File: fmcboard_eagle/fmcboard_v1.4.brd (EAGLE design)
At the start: 147 x 74 mm, 160 parts, among them IC1 OPA699ID, IC10 LTC6229IMS8E#TRPBF, IC11 7805TV, IC12 SN74AUC2G66DCTR, IC13 SN74AUC2G66DCTR, IC14 SN74AUC2G66DCTR, IC15 SN74AUC2G66DCTR, IC16 DAC7578SPWR, IC2 DAC7578SPWR, IC3 LTC6229IMS8E#TRPBF, IC4 LTC6229IMS8E#TRPBF, IC5 LM358, IC6 OPA699ID, IC7 OPA699ID, IC8 LTC6229IMS8E#TRPBF, IC9 LTC6229IMS8E#TRPBF, J1 8pin, J10 8pin, J12 4p-2.54, J2 ASP-134604-01, J3 4p-2.54, J4 4p-2.54, J5 8pin, J6 4p-2.54, J7 4p-2.54, J8 4p-2.54, J9 8pin, U1 TXS0108EPWR, U2 STMICROELECTRONICS_L7905ACVST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

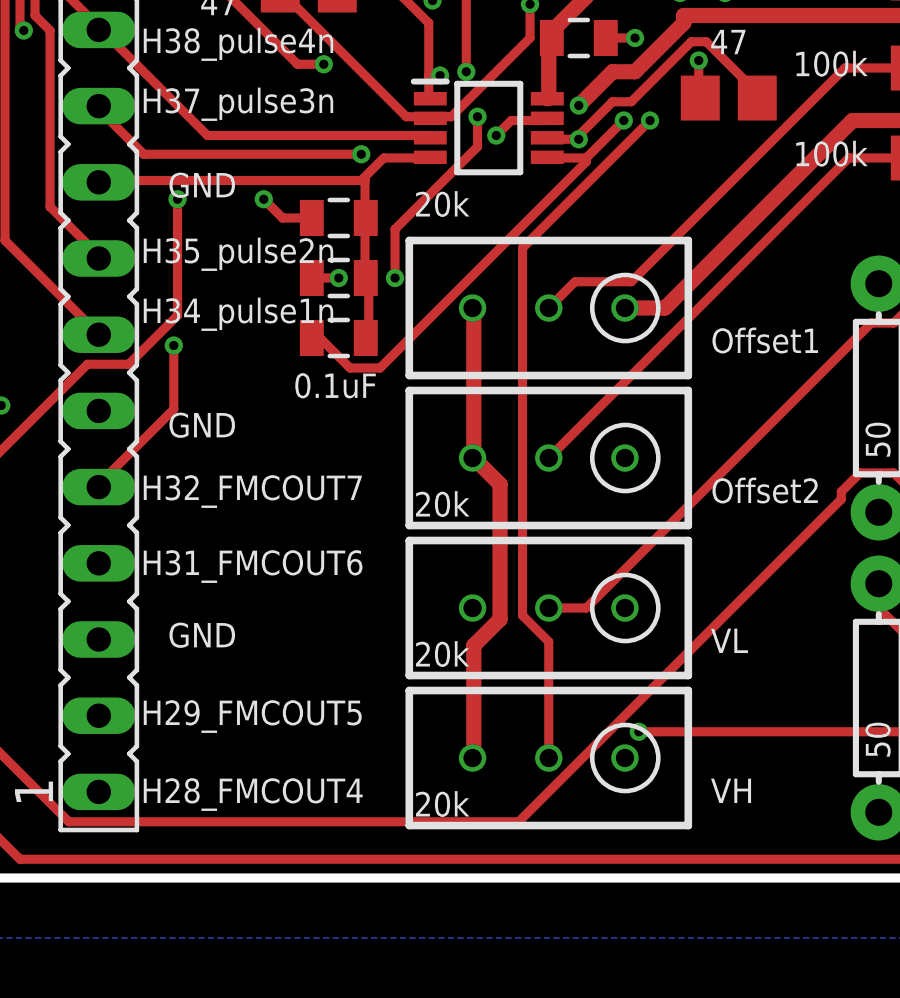
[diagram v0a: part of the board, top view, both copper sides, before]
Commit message: 20k -> 5k pots
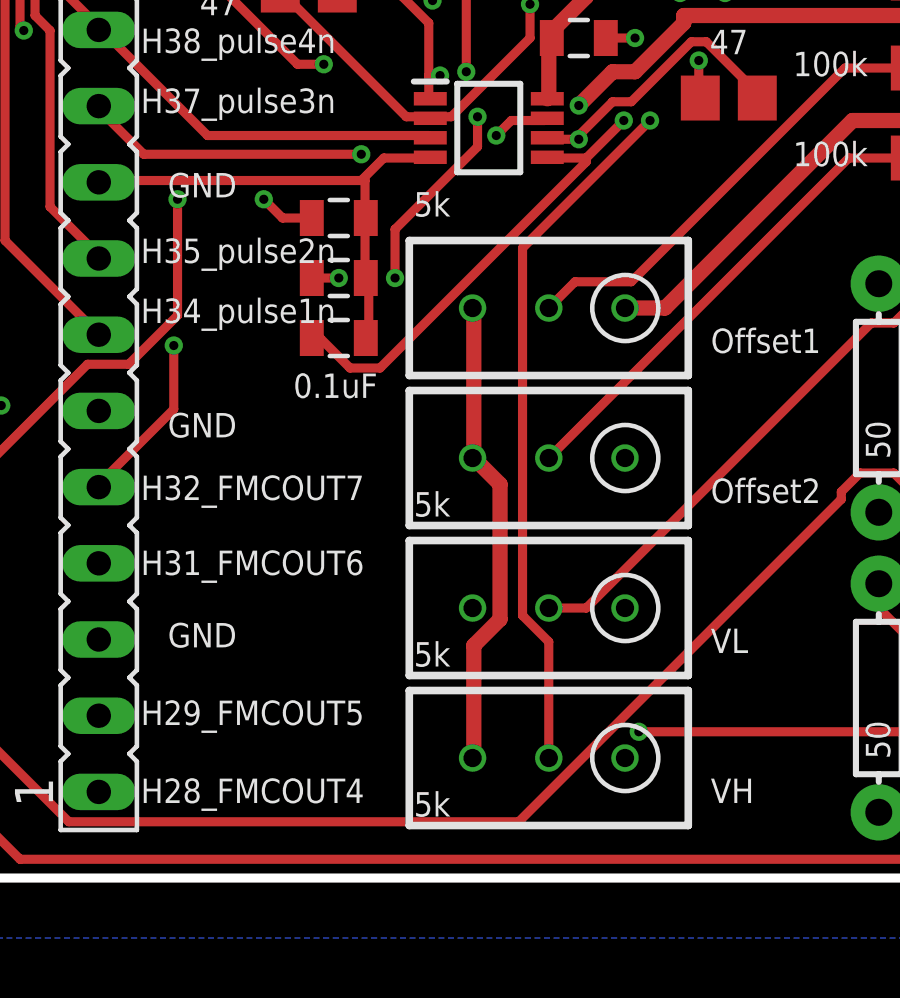
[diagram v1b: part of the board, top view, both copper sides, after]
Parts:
- R_O1, R_O2, R_VH, R_VL: value 20k -> 5k
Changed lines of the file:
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@@
 <element name="C13" library="SparkFun-Passives" package="0805" value="0.1uF" x="54" y="67" smashed="yes"/>
 <element name="C14" library="SparkFun-Passives" package="0805" value="0.1uF" x="96" y="2" smashed="yes" rot="R180"/>
-<element name="R_VH" library="resistor" library_urn="urn:adsk.eagle:library:348" package="RTRIM3296W" package3d_urn="urn:adsk.eagle:package:26033/1" value="20k" x="43" y="4" smashed="yes" rot="R90">
+<element name="R_VH" library="resistor" library_urn="urn:adsk.eagle:library:348" package="RTRIM3296W" package3d_urn="urn:adsk.eagle:package:26033/1" value="5k" x="43" y="4" smashed="yes" rot="R90">
 <attribute name="VALUE" x="38.5" y="2.05" size="0.8128" layer="21"/>
 </element>
-<element name="R_VL" library="resistor" library_urn="urn:adsk.eagle:library:348" package="RTRIM3296W" package3d_urn="urn:adsk.eagle:package:26033/1" value="20k" x="43" y="9" smashed="yes" rot="R90">
+<element name="R_VL" library="resistor" library_urn="urn:adsk.eagle:library:348" package="RTRIM3296W" package3d_urn="urn:adsk.eagle:package:26033/1" value="5k" x="43" y="9" smashed="yes" rot="R90">
 <attribute name="VALUE" x="38.5" y="7.05" size="0.8128" layer="21"/>
 </element>
@@
 <attribute name="VALUE" x="73.635" y="45.54" size="0.8128" layer="21" rot="R180"/>
 </element>
-<element name="R_O1" library="resistor" library_urn="urn:adsk.eagle:library:348" package="RTRIM3296W" package3d_urn="urn:adsk.eagle:package:26033/1" value="20k" x="43" y="19" smashed="yes" rot="R90">
+<element name="R_O1" library="resistor" library_urn="urn:adsk.eagle:library:348" package="RTRIM3296W" package3d_urn="urn:adsk.eagle:package:26033/1" value="5k" x="43" y="19" smashed="yes" rot="R90">
 <attribute name="VALUE" x="38.5" y="22.05" size="0.8128" layer="21"/>
 </element>
@@
 </element>
 <element name="C4" library="SparkFun-Passives" package="0805" value="0.1uF" x="69" y="24" smashed="yes"/>
-<element name="R_O2" library="resistor" library_urn="urn:adsk.eagle:library:348" package="RTRIM3296W" package3d_urn="urn:adsk.eagle:package:26033/1" value="20k" x="43" y="14" smashed="yes" rot="R90">
+<element name="R_O2" library="resistor" library_urn="urn:adsk.eagle:library:348" package="RTRIM3296W" package3d_urn="urn:adsk.eagle:package:26033/1" value="5k" x="43" y="14" smashed="yes" rot="R90">
 <attribute name="VALUE" x="38.5" y="12.05" size="0.8128" layer="21"/>
 </element>

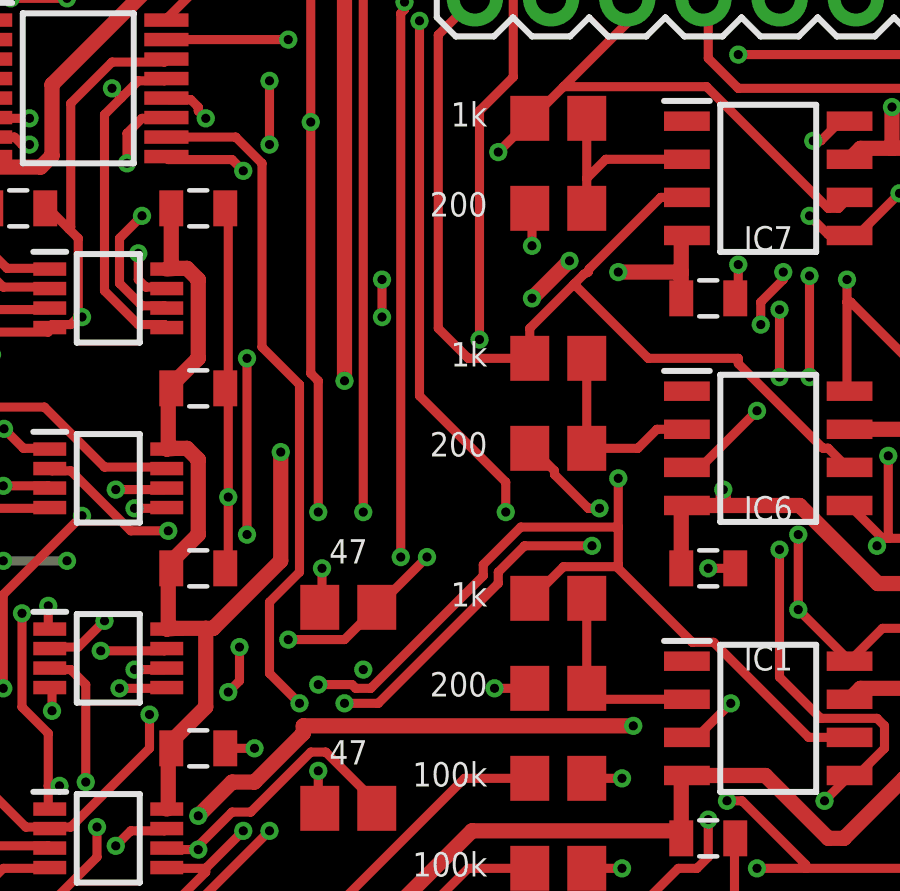
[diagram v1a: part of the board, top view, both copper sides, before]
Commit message: Gain resistors updated to 1k, 100
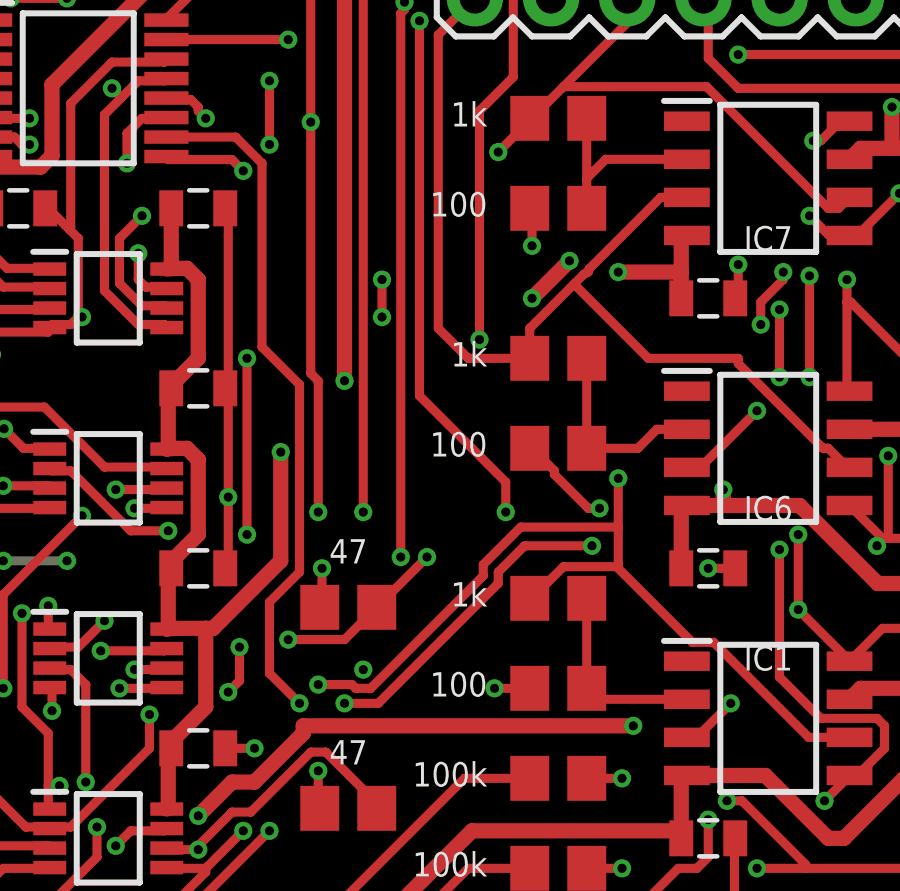
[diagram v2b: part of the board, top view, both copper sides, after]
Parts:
- R10, R19, R26: value 200 -> 100
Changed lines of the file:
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@@
 <attribute name="VALUE" x="53.635" y="33.54" size="0.8128" layer="21" rot="R180"/>
 </element>
-<element name="R10" library="rcl" library_urn="urn:adsk.eagle:library:334" package="R0805" package3d_urn="urn:adsk.eagle:package:23553/2" value="200" x="56" y="30" smashed="yes">
+<element name="R10" library="rcl" library_urn="urn:adsk.eagle:library:334" package="R0805" package3d_urn="urn:adsk.eagle:package:23553/2" value="100" x="56" y="30" smashed="yes">
 <attribute name="POPULARITY" value="85" x="56" y="30" size="1.778" layer="27" display="off"/>
 <attribute name="SPICEPREFIX" value="R" x="56" y="30" size="1.778" layer="27" display="off"/>
@@
 <attribute name="VALUE" x="53.635" y="41.54" size="0.8128" layer="21" rot="R180"/>
 </element>
-<element name="R19" library="rcl" library_urn="urn:adsk.eagle:library:334" package="R0805" package3d_urn="urn:adsk.eagle:package:23553/2" value="200" x="56" y="38" smashed="yes">
+<element name="R19" library="rcl" library_urn="urn:adsk.eagle:library:334" package="R0805" package3d_urn="urn:adsk.eagle:package:23553/2" value="100" x="56" y="38" smashed="yes">
 <attribute name="POPULARITY" value="85" x="50" y="26" size="0.8128" layer="27" display="off"/>
 <attribute name="SPICEPREFIX" value="R" x="50" y="26" size="0.8128" layer="27" display="off"/>
@@
 <attribute name="VALUE" x="53.635" y="49.54" size="0.8128" layer="21" rot="R180"/>
 </element>
-<element name="R26" library="rcl" library_urn="urn:adsk.eagle:library:334" package="R0805" package3d_urn="urn:adsk.eagle:package:23553/2" value="200" x="56" y="46" smashed="yes">
+<element name="R26" library="rcl" library_urn="urn:adsk.eagle:library:334" package="R0805" package3d_urn="urn:adsk.eagle:package:23553/2" value="100" x="56" y="46" smashed="yes">
 <attribute name="POPULARITY" value="85" x="56" y="33" size="0.8128" layer="27" display="off"/>
 <attribute name="SPICEPREFIX" value="R" x="56" y="33" size="0.8128" layer="27" display="off"/>
